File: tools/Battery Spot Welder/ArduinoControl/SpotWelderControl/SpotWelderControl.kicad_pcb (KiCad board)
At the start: 2 copper layers, 53.3 x 69.9 mm, 11 parts, among them J1 12v Power, J2 RELAY, J3 AudioJack2_Switch

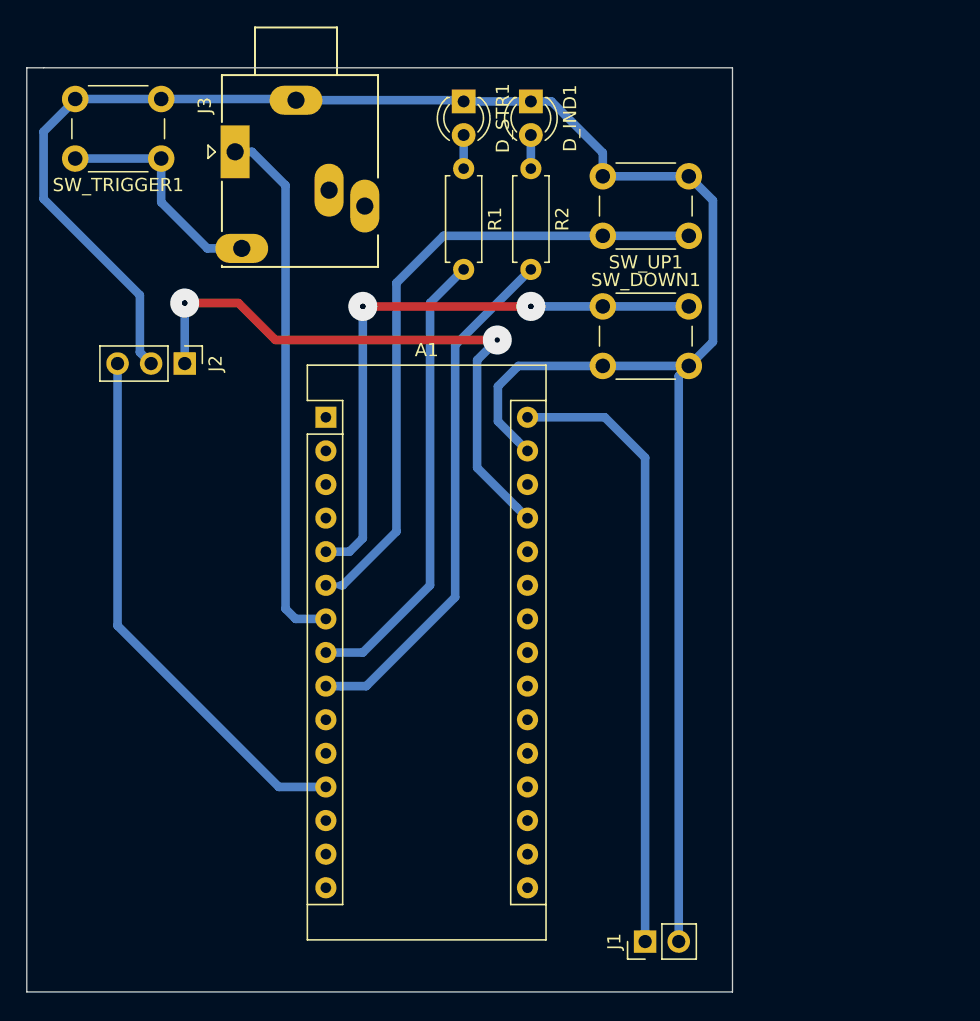
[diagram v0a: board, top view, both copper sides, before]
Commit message: Added a large capacitor to the arduino controller. Should keep voltage drop during the pulse to a minimum, and allow the controller to keep running. Added the panel buttons and relay standoff supports.
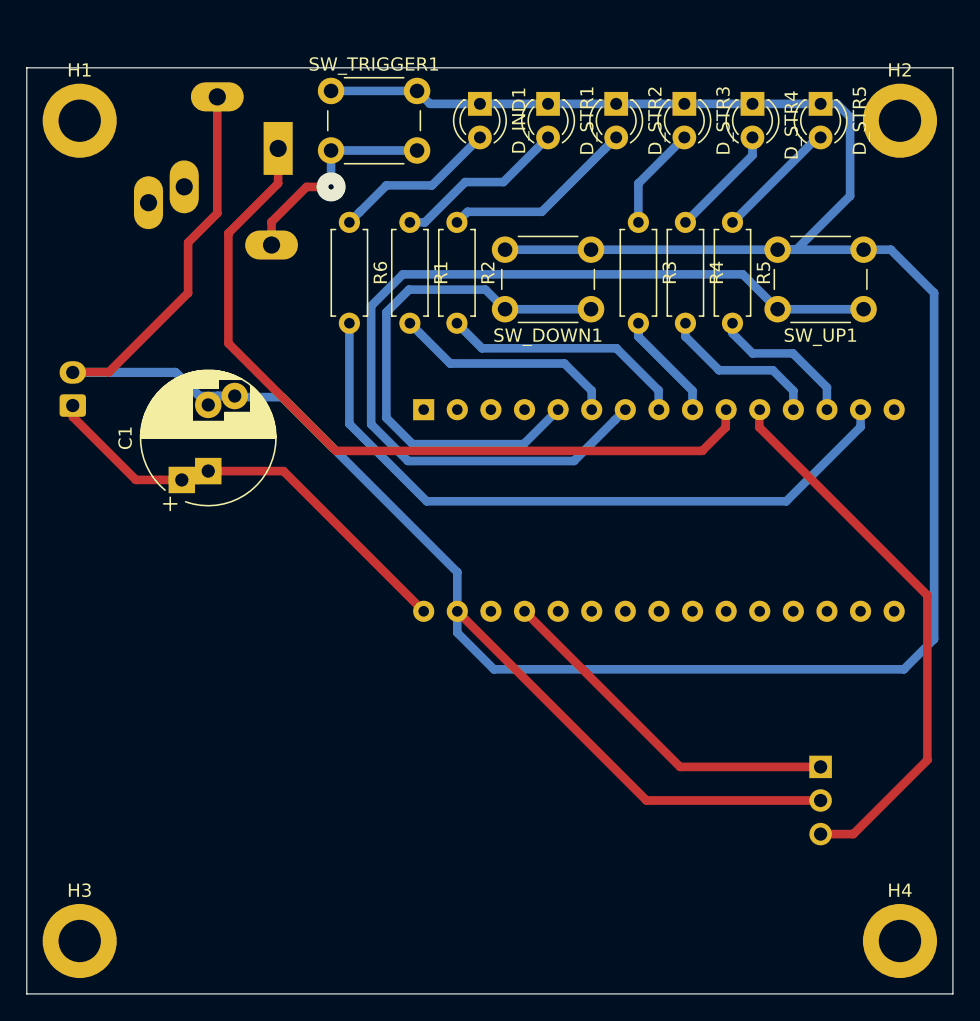
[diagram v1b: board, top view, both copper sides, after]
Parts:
- added C1: 1000uF 25VDC, Capacitor_THT:CP_Radial_D10.0mm_P5.00mm_P7.50mm, F.Cu at (138.2, 99.1)
- added D_STR2: LED, LED_THT:LED_D3.0mm, F.Cu at (169.0, 71.3)
- added D_STR3: LED, LED_THT:LED_D3.0mm, F.Cu at (174.2, 71.3)
- added D_STR4: LED, LED_THT:LED_D3.0mm, F.Cu at (179.3, 71.3)
- added D_STR5: LED, LED_THT:LED_D3.0mm, F.Cu at (184.5, 71.3)
- added H1: MountingHole, MountingHole:MountingHole_3.2mm_M3_DIN965_Pad, F.Cu at (128.5, 72.6)
- added H2: MountingHole, MountingHole:MountingHole_3.2mm_M3_DIN965_Pad, F.Cu at (190.5, 72.6)
- added H3: MountingHole, MountingHole:MountingHole_3.2mm_M3_DIN965_Pad, F.Cu at (128.5, 134.6)
- added H4: MountingHole, MountingHole:MountingHole_3.2mm_M3_DIN965_Pad, F.Cu at (190.5, 134.6)
- added R3: 1k, Resistor_THT:R_Axial_DIN0207_L6.3mm_D2.5mm_P7.62mm_Horizontal, F.Cu at (170.7, 80.3)
- added R4: 1k, Resistor_THT:R_Axial_DIN0207_L6.3mm_D2.5mm_P7.62mm_Horizontal, F.Cu at (174.2, 80.3)
- added R5: 1k, Resistor_THT:R_Axial_DIN0207_L6.3mm_D2.5mm_P7.62mm_Horizontal, F.Cu at (177.8, 80.3)
- added R6: 1k, Resistor_THT:R_Axial_DIN0207_L6.3mm_D2.5mm_P7.62mm_Horizontal, F.Cu at (148.8, 80.3)
- A1, J2, J3: moved to B.Cu
- J1: footprint Connector_PinHeader_2.54mm:PinHeader_1x02_P2.54mm_Vertical -> Connector_JST:JST_XH_B2B-XH-A_1x02_P2.50mm_Vertical; moved to B.Cu
- moved J1 59.3 mm to (127.9, 94.1)
- moved J2 56.9 mm to (184.5, 121.4), turned to 180 degrees
- moved SW_UP1 14.3 mm to (187.7, 86.8)
- moved SW_TRIGGER1 13.8 mm to (147.5, 70.3), turned to 0 degrees
- moved A1 7.42 mm to (154.5, 94.4), turned to 270 degrees
- moved R2 6.91 mm to (157.0, 80.3)
- moved D_STR1 6.38 mm to (163.9, 71.3)
- moved R1 5.75 mm to (153.4, 80.3)
- moved D_IND1 3.85 mm to (158.7, 71.3)
- moved J3 3.26 mm to (143.5, 74.7)
- moved SW_DOWN1 0.91 mm to (167.1, 86.8), turned to 180 degrees
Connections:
- A1 pad 10: (no net) -> Net-(A1-Pad10)
- A1 pad 11: (no net) -> Net-(A1-Pad11)
- A1 pad 13: (no net) -> Net-(A1-Pad13)
- A1 pad 14: (no net) -> Net-(A1-Pad14)
- J2 pad 3: Net-(A1-Pad12) -> Net-(A1-Pad11)
- J3 pad T: Net-(A1-Pad7) -> Net-(A1-Pad10)
- R1 pad 2: Net-(A1-Pad8) -> Net-(A1-Pad6)
- R2 pad 1: Net-(D_IND1-Pad2) -> Net-(D_STR2-Pad2)
- R2 pad 2: Net-(A1-Pad9) -> Net-(A1-Pad8)
- SW_TRIGGER1 pad 1: Net-(J3-PadTN) -> GND
- SW_TRIGGER1 pad 2: GND -> Net-(J3-PadTN)
- SW_UP1 pad 1: Net-(A1-Pad6) -> Net-(A1-Pad7)
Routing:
- net GND: track 154.7 -> 265.0 mm
- net Net-(A1-Pad10): track 0.00 -> 59.3 mm
- net Net-(A1-Pad14): track 0.00 -> 52.3 mm
- net Net-(A1-Pad11): track 0.00 -> 42.1 mm
- net Net-(A1-Pad6): track 49.4 -> 17.3 mm
- net Net-(A1-Pad9): track 39.7 -> 8.23 mm
- net Net-(A1-Pad7): track 40.2 -> 70.2 mm
- net Net-(A1-Pad12): track 40.6 -> 12.3 mm
- net Net-(A1-Pad27): track 45.0 -> 27.3 mm, vias 3 -> 0
- net +12V: track 51.6 -> 34.0 mm
- net Net-(A1-Pad8): track 34.9 -> 18.8 mm
- net Net-(D_STR2-Pad2): track 0.00 -> 14.7 mm
- net Net-(A1-Pad13): track 0.00 -> 11.3 mm
- net Net-(D_STR1-Pad2): track 2.54 -> 13.1 mm
- net Net-(D_IND1-Pad2): track 2.54 -> 12.5 mm
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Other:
- board size 53.3 x 69.9 mm -> 70 x 70 mm
